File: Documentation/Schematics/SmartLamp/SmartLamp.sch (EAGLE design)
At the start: 31 parts, among them J1 POWER_JACKPTH_BREAD, J2 AVR_SPI_PROG_5X2PTH2, Q1 STN4NF03L, Q2 STN4NF03L, Q3 STN4NF03L, U1 MIC2920A, U2 DS3231MZ, U3 ATMEGA8/168/328, U4 HM-10

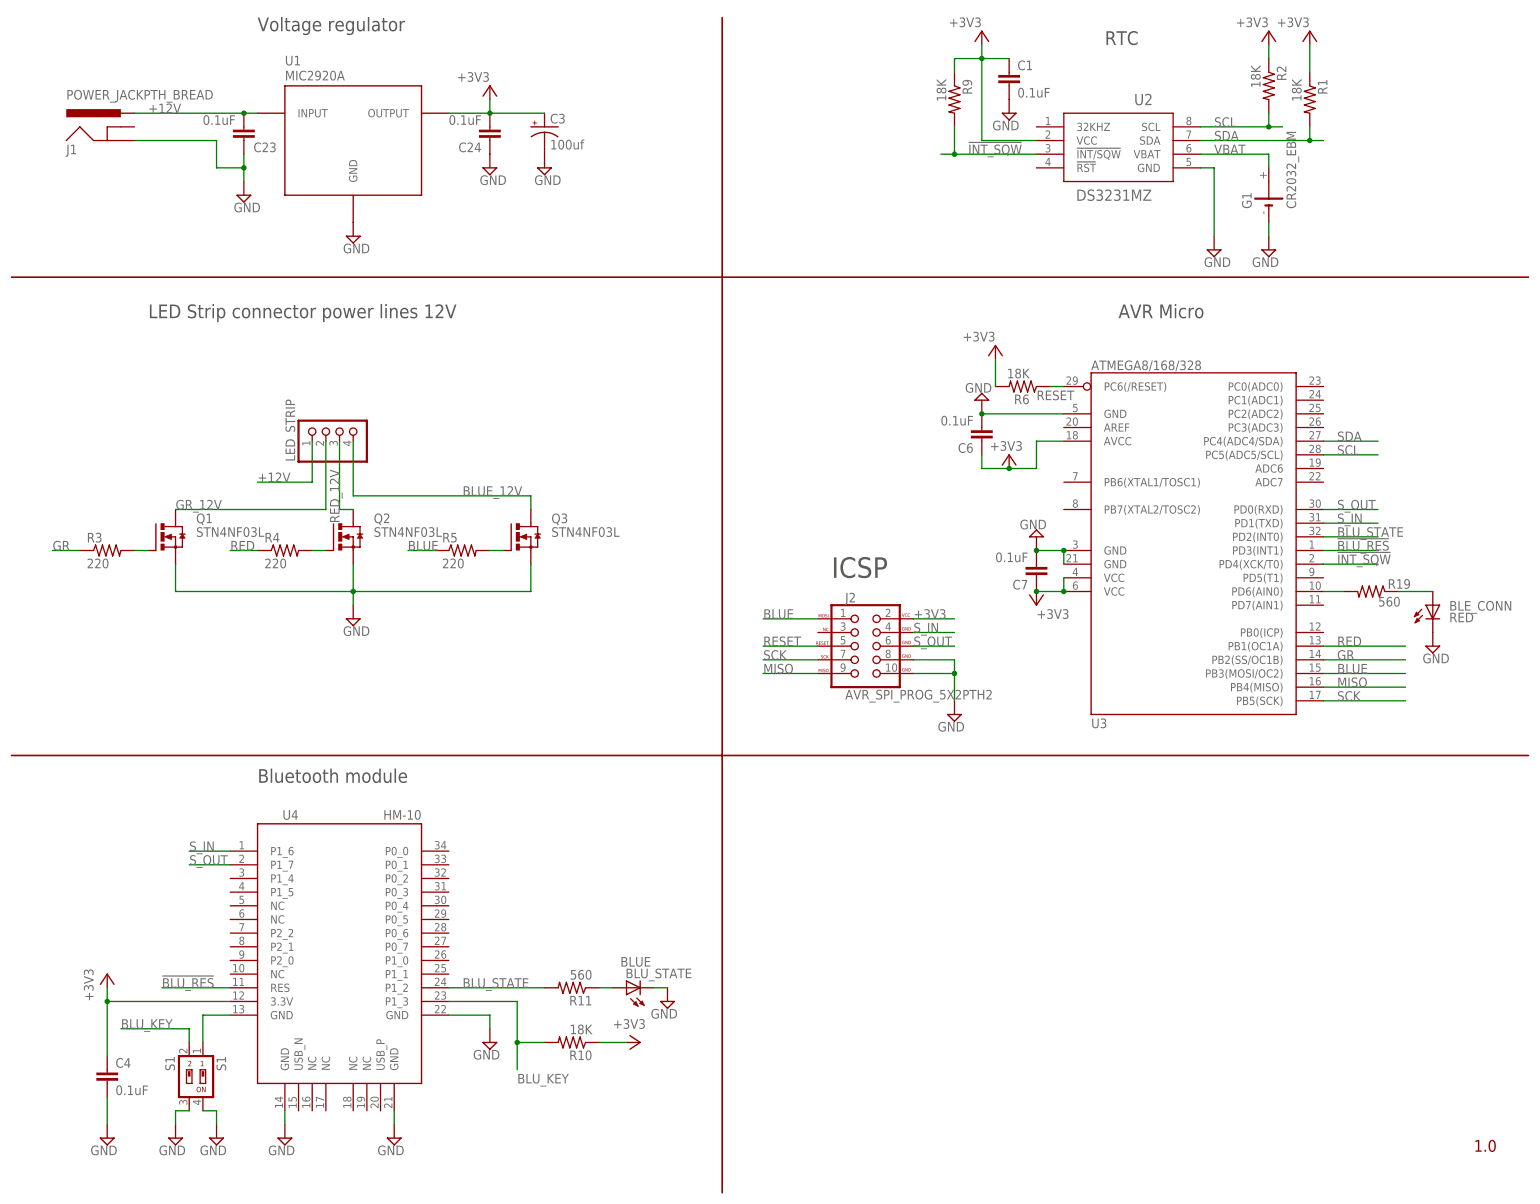
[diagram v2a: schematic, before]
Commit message: Fixed DC jack and battery holder footprint.. milling level needed for slot holes.
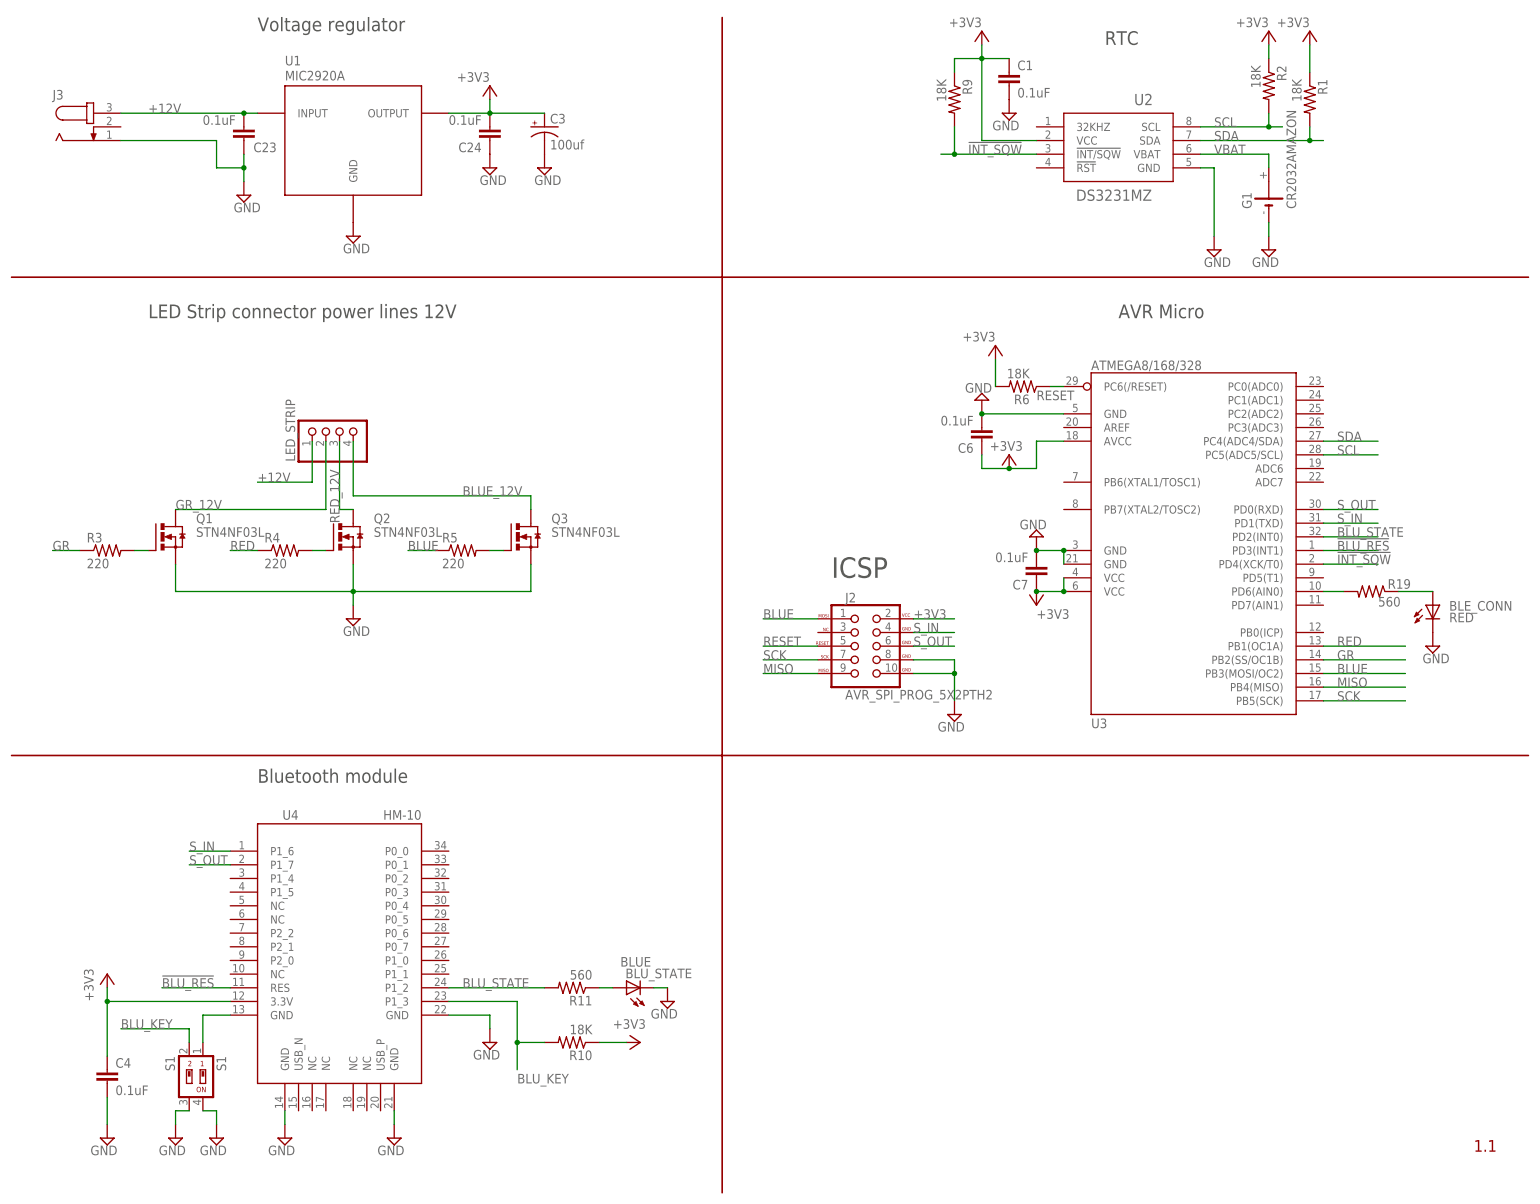
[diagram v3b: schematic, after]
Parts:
- removed J1: POWER_JACKPTH_BREAD, SparkFun-Connectors:POWER_JACKPTH_BREAD
- added J3: (no value), con-jack:JACK-PLUG0
- G1: value CR2032_EBM -> CR2032AMAZON; device CuSTOM_GB:CR2032_EBM -> CuSTOM_GB:CR2032AMAZON
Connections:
- net +12V: now also J3.3; no longer J1.PWR
- net GND: now also J3.1; no longer J1.GND
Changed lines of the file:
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@@
 <grid distance="0.1" unitdist="inch" unit="inch" style="lines" multiple="1" display="no" altdistance="0.01" altunitdist="inch" altunit="inch"/>
 <layers>
-<layer number="1" name="Top" color="4" fill="1" visible="no" active="no"/>
-<layer number="16" name="Bottom" color="1" fill="1" visible="no" active="no"/>
-<layer number="17" name="Pads" color="2" fill="1" visible="no" active="no"/>
-<layer number="18" name="Vias" color="2" fill="1" visible="no" active="no"/>
-<layer number="19" name="Unrouted" color="6" fill="1" visible="no" active="no"/>
-<layer number="20" name="Dimension" color="15" fill="1" visible="no" active="no"/>
-<layer number="21" name="tPlace" color="7" fill="1" visible="no" active="no"/>
-<layer number="22" name="bPlace" color="7" fill="1" visible="no" active="no"/>
-<layer number="23" name="tOrigins" color="15" fill="1" visible="no" active="no"/>
-<layer number="24" name="bOrigins" color="15" fill="1" visible="no" active="no"/>
-<layer number="25" name="tNames" color="7" fill="1" visible="no" active="no"/>
-<layer number="26" name="bNames" color="7" fill="1" visible="no" active="no"/>
-<layer number="27" name="tValues" color="7" fill="1" visible="no" active="no"/>
-<layer number="28" name="bValues" color="7" fill="1" visible="no" active="no"/>
+<layer number="1" name="Top" color="4" fill="1" visible="yes" active="no"/>
+<layer number="16" name="Bottom" color="1" fill="1" visible="yes" active="no"/>
+<layer number="17" name="Pads" color="2" fill="1" visible="yes" active="no"/>
+<layer number="18" name="Vias" color="2" fill="1" visible="yes" active="no"/>
+<layer number="19" name="Unrouted" color="6" fill="1" visible="yes" active="no"/>
+<layer number="20" name="Dimension" color="15" fill="1" visible="yes" active="no"/>
+<layer number="21" name="tPlace" color="7" fill="1" visible="yes" active="no"/>
+<layer number="22" name="bPlace" color="7" fill="1" visible="yes" active="no"/>
+<layer number="23" name="tOrigins" color="15" fill="1" visible="yes" active="no"/>
+<layer number="24" name="bOrigins" color="15" fill="1" visible="yes" active="no"/>
+<layer number="25" name="tNames" color="7" fill="1" visible="yes" active="no"/>
+<layer number="26" name="bNames" color="7" fill="1" visible="yes" active="no"/>
+<layer number="27" name="tValues" color="7" fill="1" visible="yes" active="no"/>
+<layer number="28" name="bValues" color="7" fill="1" visible="yes" active="no"/>
 <layer number="29" name="tStop" color="7" fill="3" visible="no" active="no"/>
 <layer number="30" name="bStop" color="7" fill="6" visible="no" active="no"/>
@@
 <layer number="35" name="tGlue" color="7" fill="4" visible="no" active="no"/>
 <layer number="36" name="bGlue" color="7" fill="5" visible="no" active="no"/>
-<layer number="37" name="tTest" color="7" fill="1" visible="no" active="no"/>
-<layer number="38" name="bTest" color="7" fill="1" visible="no" active="no"/>
+<layer number="37" name="tTest" color="7" fill="1" visible="yes" active="no"/>
+<layer number="38" name="bTest" color="7" fill="1" visible="yes" active="no"/>
 <layer number="39" name="tKeepout" color="4" fill="11" visible="no" active="no"/>
 <layer number="40" name="bKeepout" color="1" fill="11" visible="no" active="no"/>
@@
 <layer number="44" name="Drills" color="7" fill="1" visible="no" active="no"/>
 <layer number="45" name="Holes" color="7" fill="1" visible="no" active="no"/>
-<layer number="46" name="Milling" color="3" fill="1" visible="no" active="no"/>
-<layer number="47" name="Measures" color="7" fill="1" visible="no" active="no"/>
-<layer number="48" name="Document" color="7" fill="1" visible="no" active="no"/>
-<layer number="49" name="Reference" color="7" fill="1" visible="no" active="no"/>
-<layer number="50" name="dxf" color="7" fill="1" visible="no" active="no"/>
-<layer number="51" name="tDocu" color="7" fill="1" visible="no" active="no"/>
-<layer number="52" name="bDocu" color="7" fill="1" visible="no" active="no"/>
-<layer number="53" name="tGND_GNDA" color="7" fill="9" visible="no" active="no"/>
-<layer number="54" name="bGND_GNDA" color="1" fill="9" visible="no" active="no"/>
-<layer number="56" name="wert" color="7" fill="1" visible="no" active="no"/>
-<layer number="57" name="tCAD" color="7" fill="1" visible="no" active="no"/>
-<layer number="59" name="tCarbon" color="7" fill="1" visible="no" active="no"/>
-<layer number="60" name="bCarbon" color="7" fill="1" visible="no" active="no"/>
+<layer number="46" name="Milling" color="3" fill="1" visible="yes" active="no"/>
+<layer number="47" name="Measures" color="7" fill="1" visible="yes" active="no"/>
+<layer number="48" name="Document" color="7" fill="1" visible="yes" active="no"/>
+<layer number="49" name="Reference" color="7" fill="1" visible="yes" active="no"/>
+<layer number="50" name="dxf" color="7" fill="1" visible="yes" active="no"/>
+<layer number="51" name="tDocu" color="7" fill="1" visible="yes" active="no"/>
+<layer number="52" name="bDocu" color="7" fill="1" visible="yes" active="no"/>
+<layer number="53" name="tGND_GNDA" color="7" fill="9" visible="yes" active="no"/>
+<layer number="54" name="bGND_GNDA" color="1" fill="9" visible="yes" active="no"/>
+<layer number="56" name="wert" color="7" fill="1" visible="yes" active="no"/>
+<layer number="57" name="tCAD" color="7" fill="1" visible="yes" active="no"/>
+<layer number="59" name="tCarbon" color="7" fill="1" visible="yes" active="no"/>
+<layer number="60" name="bCarbon" color="7" fill="1" visible="yes" active="no"/>
 <layer number="90" name="Modules" color="5" fill="1" visible="yes" active="yes"/>
 <layer number="91" name="Nets" color="2" fill="1" visible="yes" active="yes"/>
@@
 <schematic xreflabel="%F%N/%S" xrefpart="/%S.%C%R">
 <attributes>
-<attribute name="VERSION" value="1.0"/>
+<attribute name="VERSION" value="1.1"/>
 </attributes>
 <variantdefs>
@@
 <part name="R1" library="rcl" deviceset="R-US_" device="R1206" value="18K"/>
 <part name="GND4" library="supply2" deviceset="GND" device=""/>
-<part name="J1" library="SparkFun-Connectors" deviceset="POWER_JACK" device="PTH_BREAD"/>
 <part name="C1" library="rcl" deviceset="C-EU" device="C1206" value="0.1uF"/>
 <part name="GND13" library="supply2" deviceset="GND" device=""/>
@@
 <part name="+3V3" library="supply1" deviceset="+3V3" device=""/>
 <part name="+3V4" library="supply1" deviceset="+3V3" device=""/>
-<part name="G1" library="CuSTOM_GB" deviceset="CR2032_EBM" device=""/>
+<part name="G1" library="CuSTOM_GB" deviceset="CR2032" device="AMAZON"/>
 <part name="U2" library="Maxim_RTC" deviceset="DS3231MZ" device=""/>
 <part name="R9" library="rcl" deviceset="R-US_" device="R1206" value="18K"/>
@@
 <part name="J2" library="SparkFun-Connectors" deviceset="AVR_SPI_PROG_5X2" device="PTH2"/>
 <part name="GND5" library="supply2" deviceset="GND" device=""/>
+<part name="J3" library="con-jack" deviceset="JACK-PLUG" device="0"/>
 </parts>
 <sheets>
@@
 <instance part="R1" gate="G$1" x="322.58" y="208.28" rot="R270"/>
 <instance part="GND4" gate="GND" x="266.7" y="205.74" rot="MR0"/>
-<instance part="J1" gate="G$1" x="101.6" y="198.12"/>
 <instance part="C1" gate="G$1" x="266.7" y="213.36"/>
 <instance part="GND13" gate="GND" x="314.96" y="180.34" rot="MR0"/>
@@
 <instance part="J2" gate="G$1" x="238.76" y="106.68"/>
 <instance part="GND5" gate="GND" x="256.54" y="93.98" rot="MR0"/>
+<instance part="J3" gate="G$1" x="96.52" y="203.2"/>
 </instances>
 <busses>
@@
 <wire x1="124.46" y1="198.12" x2="124.46" y2="195.58" width="0.1524" layer="91"/>
 <junction x="124.46" y="195.58"/>
-<pinref part="J1" gate="G$1" pin="GND"/>
-<wire x1="104.14" y1="200.66" x2="119.38" y2="200.66" width="0.1524" layer="91"/>
 <wire x1="119.38" y1="200.66" x2="119.38" y2="195.58" width="0.1524" layer="91"/>
 <wire x1="119.38" y1="195.58" x2="124.46" y2="195.58" width="0.1524" layer="91"/>
+<pinref part="J3" gate="G$1" pin="1"/>
+<wire x1="119.38" y1="200.66" x2="101.6" y2="200.66" width="0.1524" layer="91"/>
 </segment>
 <segment>
@@
 </segment>
 <segment>
-<pinref part="J1" gate="G$1" pin="PWR"/>
-<wire x1="104.14" y1="205.74" x2="124.46" y2="205.74" width="0.1524" layer="91"/>
 <label x="106.68" y="205.74" size="1.778" layer="95" font="vector"/>
 <pinref part="C23" gate="G$1" pin="2"/>
 <wire x1="124.46" y1="205.74" x2="127" y2="205.74" width="0.1524" layer="91"/>
+<pinref part="U1" gate="G$1" pin="INPUT"/>
+<pinref part="J3" gate="G$1" pin="3"/>
+<wire x1="101.6" y1="205.74" x2="124.46" y2="205.74" width="0.1524" layer="91"/>
 <junction x="124.46" y="205.74"/>
-<pinref part="U1" gate="G$1" pin="INPUT"/>
-</segment>
-</net>
+</segment>
+</net>
